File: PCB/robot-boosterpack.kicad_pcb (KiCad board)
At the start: 2 copper layers, 57 parts, among them IC1 DRV8833, IC2 TPS77033, IC3 TPS77050, IC4 LMR61428, J1 3.3V Jumper, J2 5V Jumper, J3 9V Jumper, M1 MOTOR, M2 MOTOR

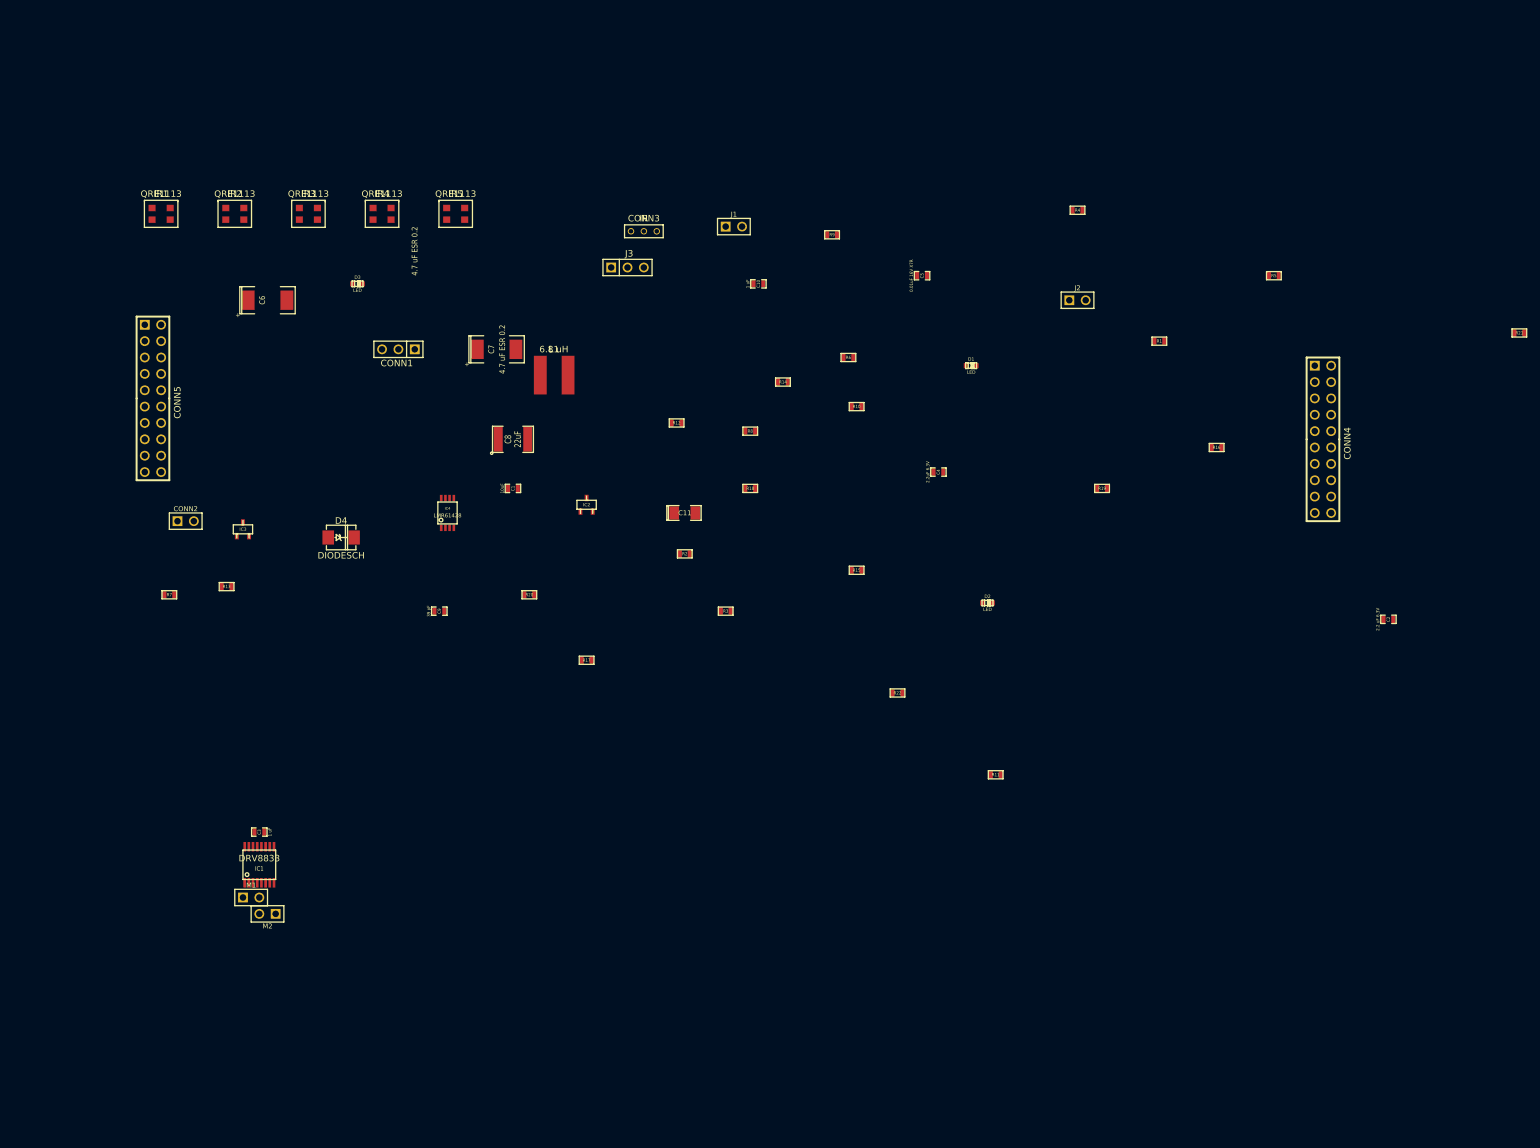
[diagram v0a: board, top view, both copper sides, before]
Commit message: added pcb outline
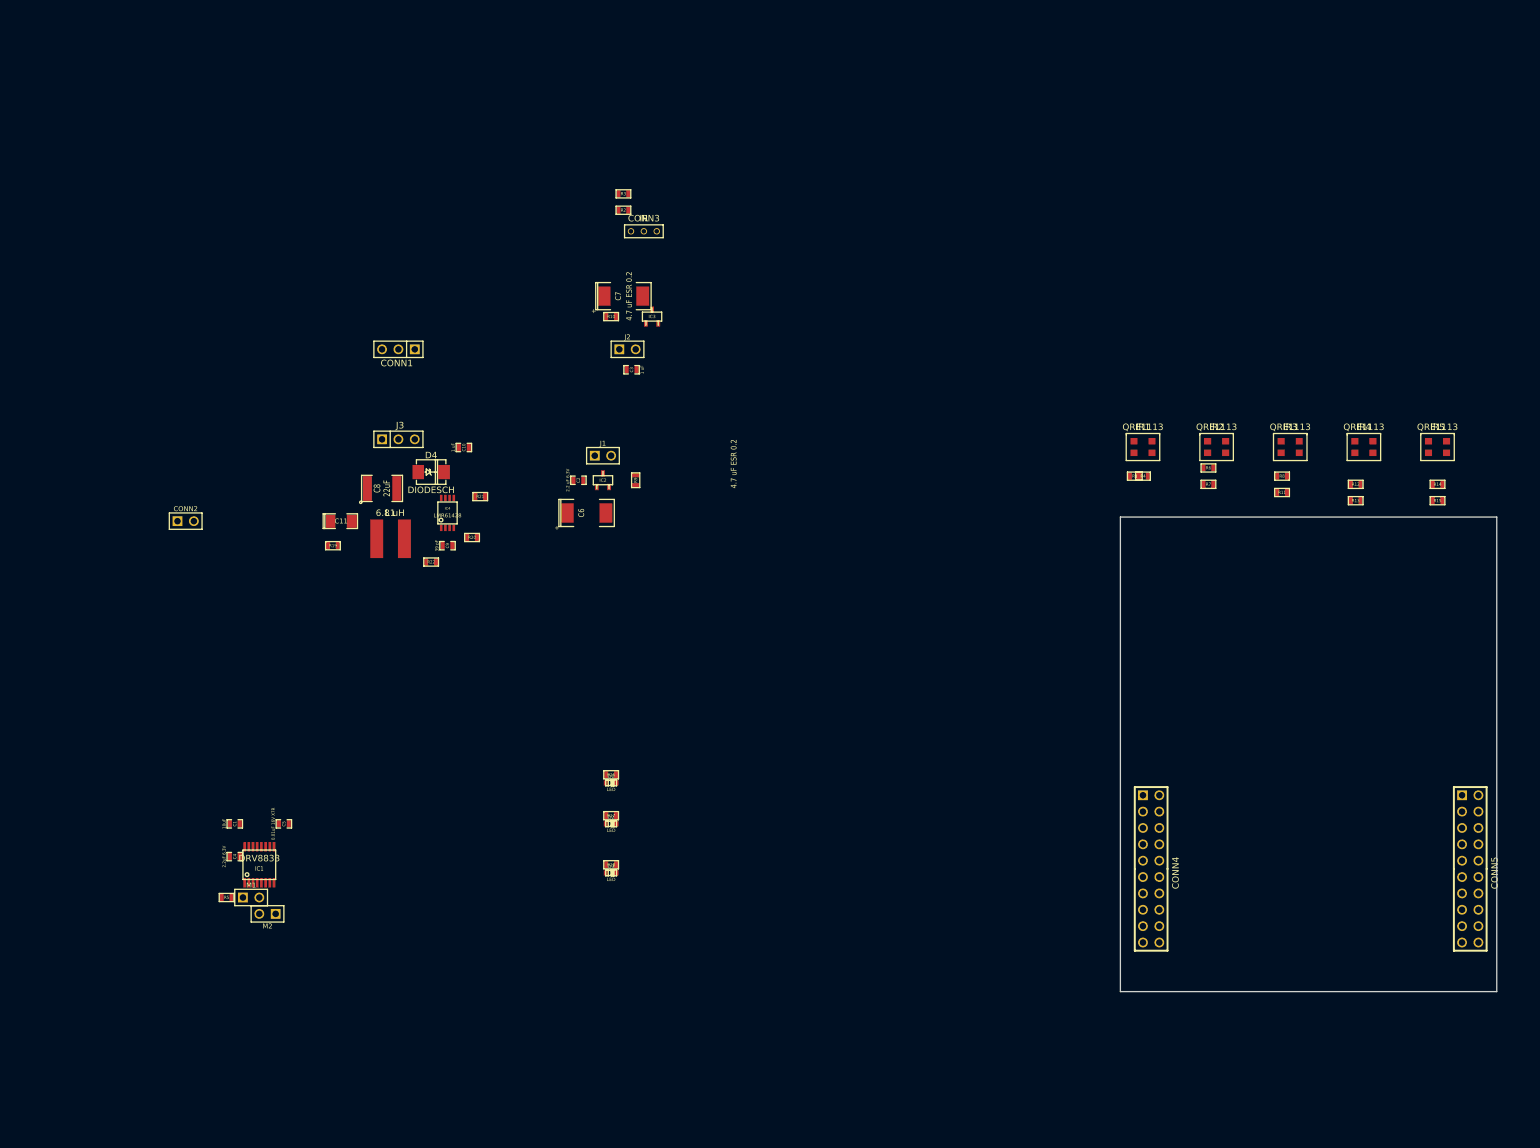
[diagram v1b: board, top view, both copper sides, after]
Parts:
- moved CONN5 217.1 mm to (223.5, 120.0)
- moved R5 189.1 mm to (30.5, 124.5)
- moved R13 175.8 mm to (205.7, 62.9)
- moved R21 163.3 mm to (69.8, 62.2)
- moved R7 162.2 mm to (182.9, 60.3)
- moved IR1 156.6 mm to (172.7, 51.4)
- moved IR2 156.6 mm to (184.2, 51.4)
- moved IR3 156.6 mm to (195.6, 51.4)
- moved IR4 156.6 mm to (207.0, 51.4)
- moved IR5 156.6 mm to (218.4, 51.4)
- moved C5 130.6 mm to (39.4, 113.0)
- moved C2 127.6 mm to (85.1, 59.7)
- moved C4 124.5 mm to (31.8, 118.1)
- moved R19 119.7 mm to (47.0, 69.8)
- moved R16 106.8 mm to (90.2, 105.4)
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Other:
- board outline added: 58.4 x 73.7 mm

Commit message: organized pcb components
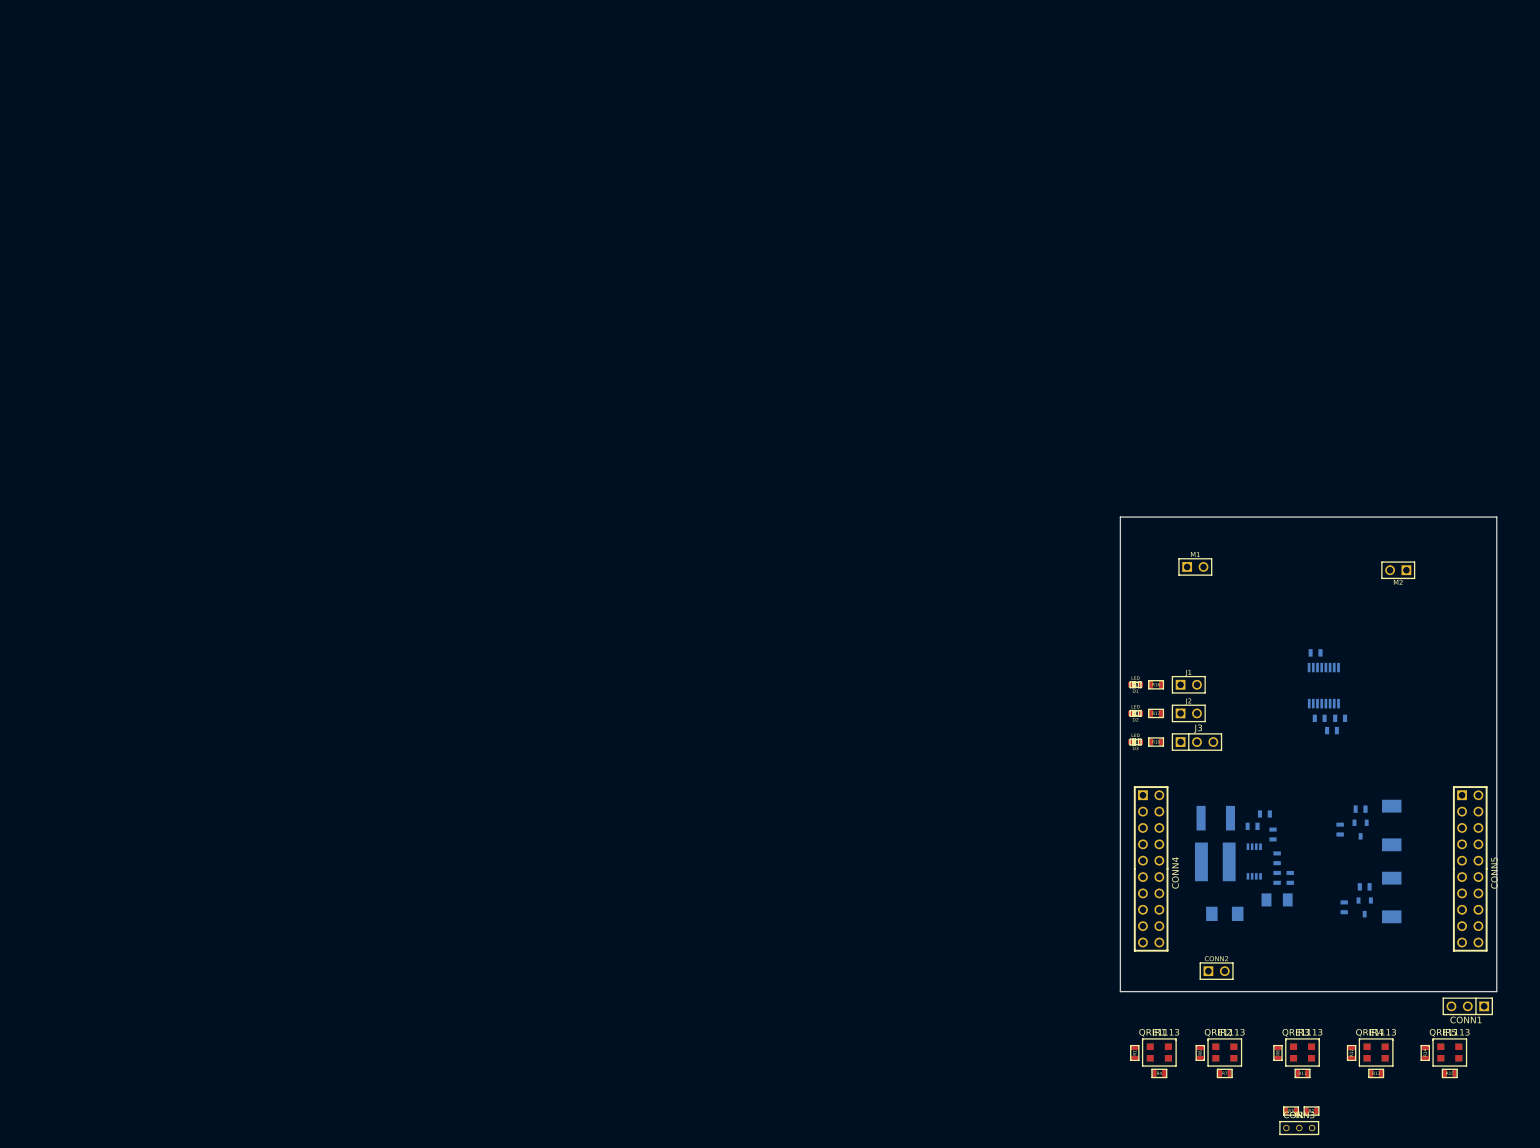
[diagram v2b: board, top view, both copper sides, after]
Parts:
- C1, C10, C11, C2, C3, C4, C5, C6, C7, C8, C9, D4, IC1, IC2, IC3, IC4, L1, R10, R19, R20, R21, R22, R5, R9: moved to B.Cu
- moved CONN1 194.8 mm to (223.1, 141.4)
- moved M2 183.4 mm to (212.3, 73.7)
- moved R3 176.1 mm to (195.7, 157.6)
- moved R2 176.0 mm to (198.9, 157.6), turned to 180 degrees
- moved CONN2 174.6 mm to (184.2, 135.9)
- moved R5 173.2 mm to (199.5, 86.5), turned to 180 degrees
- moved CONN3 172.4 mm to (197.0, 158.2)
- moved C1 170.9 mm to (202.1, 98.6)
- moved C4 169.8 mm to (200.2, 96.6)
- moved IC1 167.6 mm to (200.8, 91.6)
- moved C5 164.8 mm to (203.3, 96.6), turned to 180 degrees
- moved C11 156.7 mm to (193.5, 124.8)
- moved M1 155.3 mm to (180.8, 73.2)
- moved C7 151.4 mm to (211.3, 124.5), turned to 270 degrees
- moved R19 149.2 mm to (189.7, 113.4)
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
